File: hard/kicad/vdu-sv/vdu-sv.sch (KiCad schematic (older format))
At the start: 36 parts, among them J1 IOx, J2 (S)VGA, J3 IOx, U1 74HC138, U10 74HC245, U11 74HC245, U12 74HC245, U13 74HC574, U14 74HC157, U15 74HC86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

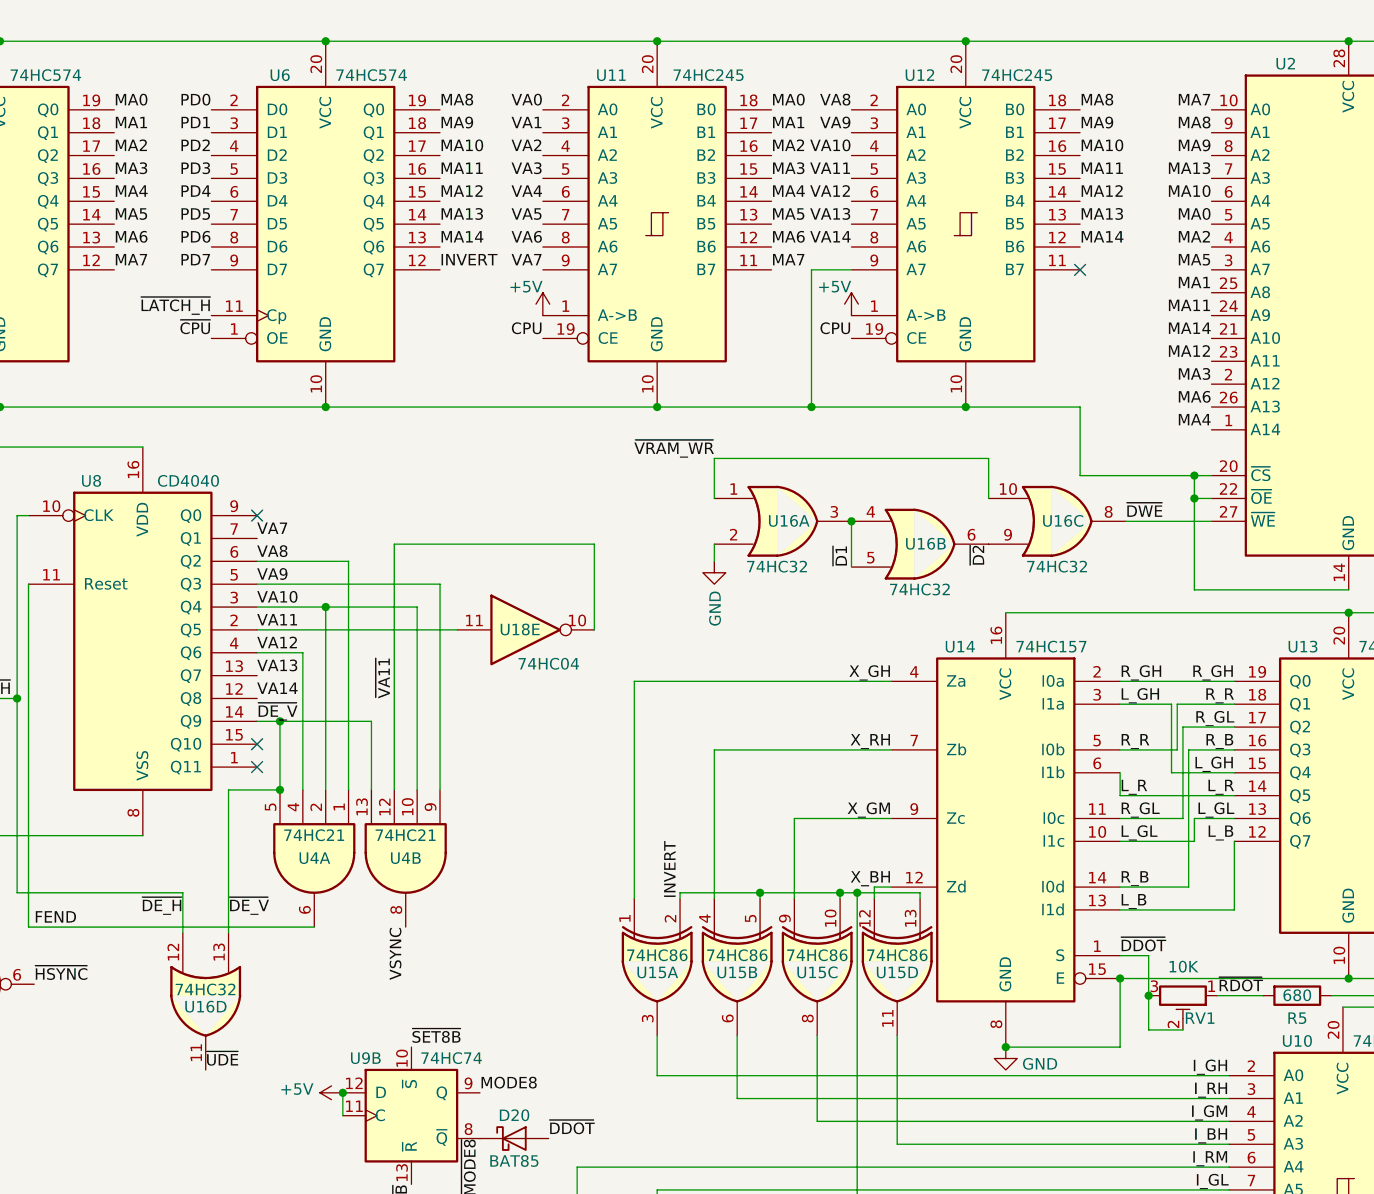
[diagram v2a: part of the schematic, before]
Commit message: upper nybble inverter shuffling
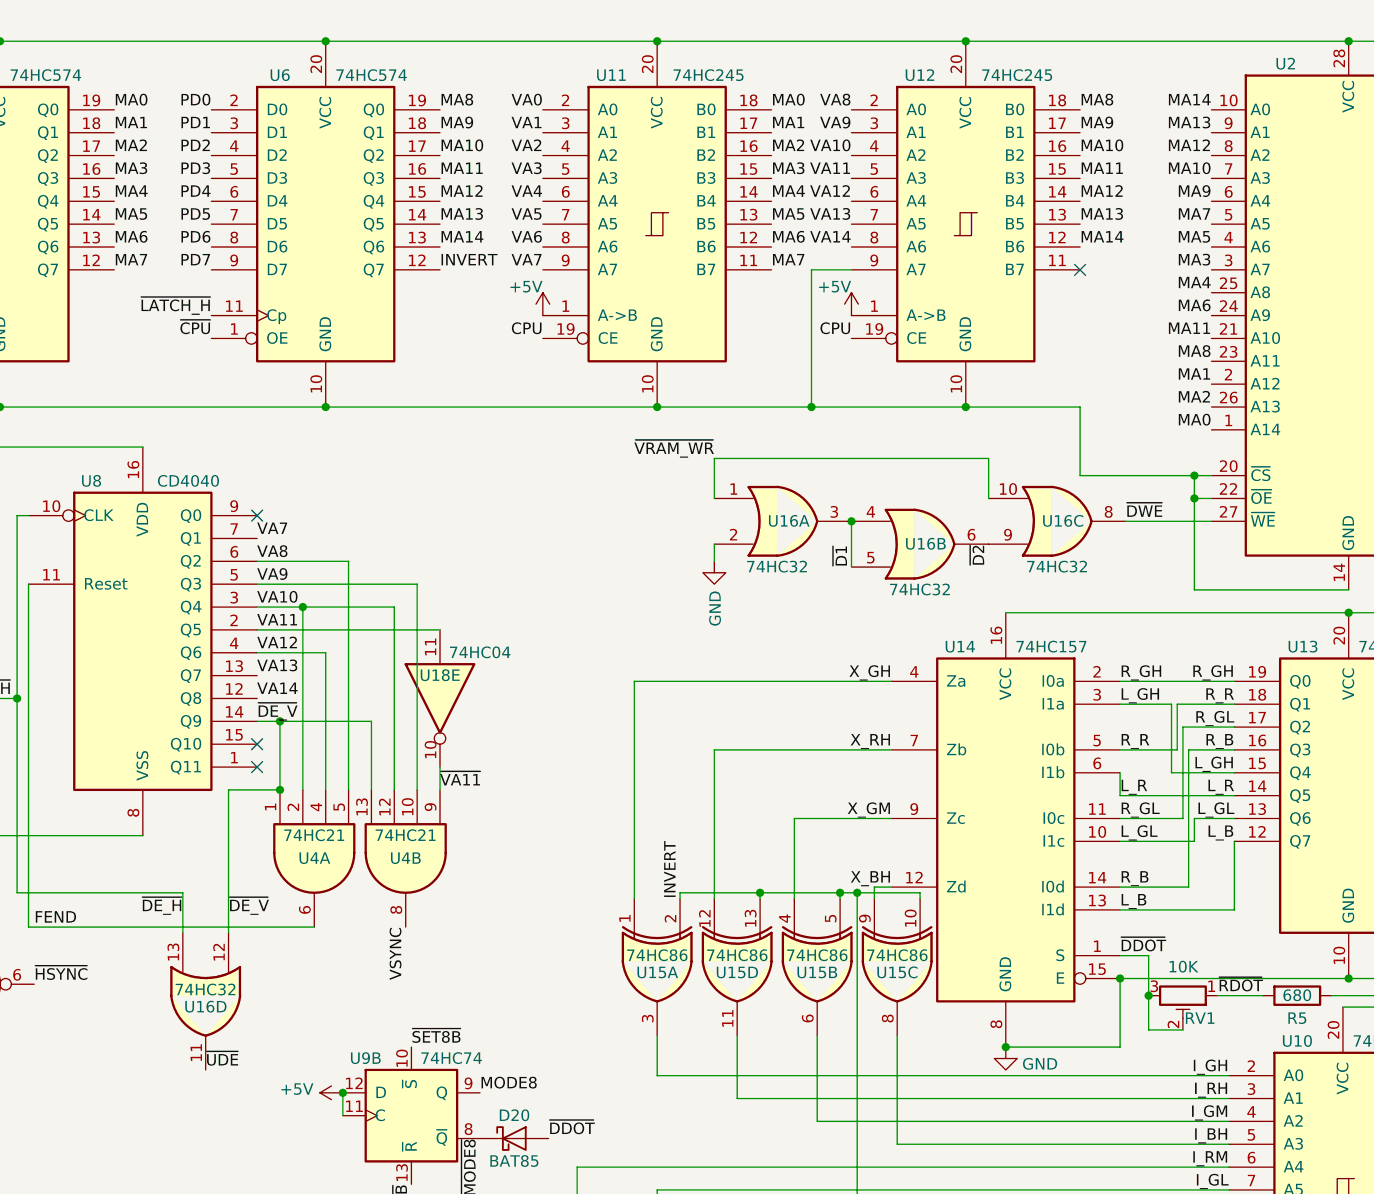
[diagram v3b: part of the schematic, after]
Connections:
- net I_BH: now also U15.8; no longer U15.11
- net I_GM: now also U15.6; no longer U15.8
- net I_RH: now also U15.11; no longer U15.6
- net MA0: now also U2.1 (A14); no longer U2.5 (A5)
- net MA1: now also U2.2 (A12); no longer U2.25 (A8)
- net MA10: now also U2.7 (A3); no longer U2.6 (A4)
- net MA11: now also U2.21 (A10); no longer U2.24 (A9)
- net MA12: now also U2.8 (A2); no longer U2.23 (A11)
- net MA13: now also U2.9 (A1); no longer U2.7 (A3)
- net MA14: now also U2.10 (A0); no longer U2.21 (A10)
- net MA2: now also U2.26 (A13); no longer U2.4 (A6)
- net MA3: now also U2.3 (A7); no longer U2.2 (A12)
- net MA4: now also U2.25 (A8); no longer U2.1 (A14)
- net MA5: now also U2.4 (A6); no longer U2.3 (A7)
- net MA6: now also U2.24 (A9); no longer U2.26 (A13)
- net MA7: now also U2.5 (A5); no longer U2.10 (A0)
- net MA8: now also U2.23 (A11); no longer U2.9 (A1)
- net MA9: now also U2.6 (A4); no longer U2.8 (A2)
- net VA10: now also U4.12; no longer U4.10
- net VA8: now also U4.5; no longer U4.1
- net VA9: now also U4.10; no longer U4.9
- net X_BH: now also U15.9; no longer U15.12
- net X_GM: now also U15.4; no longer U15.9
- net X_RH: now also U15.12; no longer U15.4
- net ~DE_H: now also U16.13; no longer U16.12
- net ~DE_V: now also U16.12, U4.1; no longer U16.13, U4.5
- net ~VA11: now also U4.9; no longer U4.12
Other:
- moved on the sheet: U15B, U15C, U15D, U18E

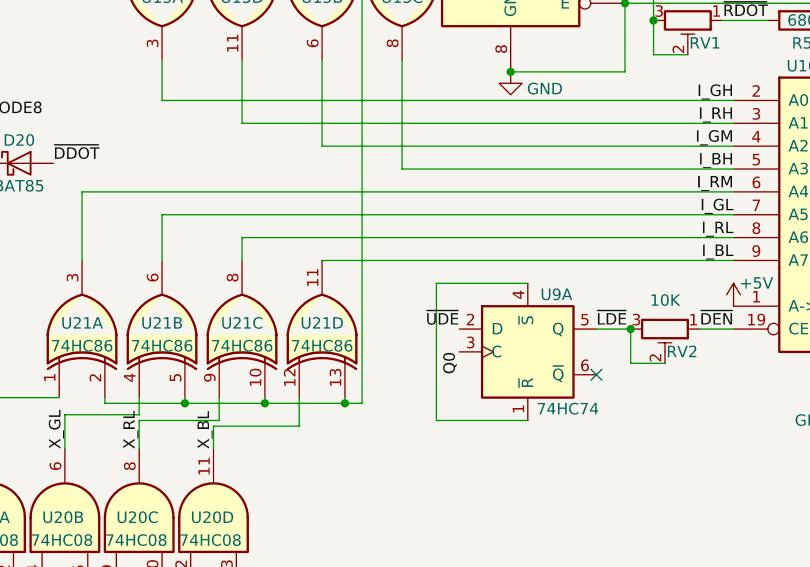
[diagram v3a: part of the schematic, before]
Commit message: somewhat more compact VDU-SV
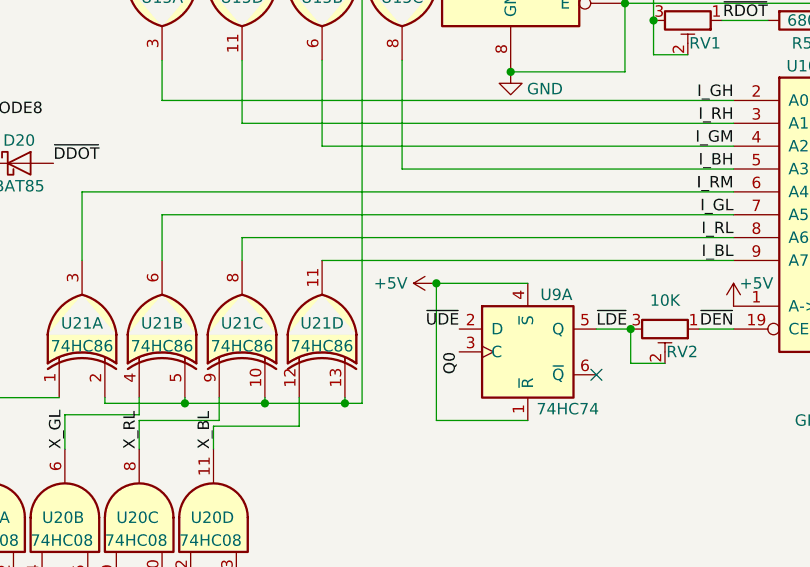
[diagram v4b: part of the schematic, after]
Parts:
- D20: footprint Diode_THT:D_DO-35_SOD27_P7.62mm_Horizontal -> Diode_THT:D_DO-35_SOD27_P2.54mm_Vertical_KathodeUp
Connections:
- net +5V: now also U9.1 (~R), U9.4 (~S)
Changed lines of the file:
@@
 F 0 "D20" H 5975 5475 50  0000 C CNN
 F 1 "BAT85" H 5975 5275 50  0000 C CNN
-F 2 "Diode_THT:D_DO-35_SOD27_P7.62mm_Horizontal" H 5975 5200 50  0001 C CNN
+F 2 "Diode_THT:D_DO-35_SOD27_P2.54mm_Vertical_KathodeUp" H 5975 5200 50  0001 C CNN
 F 3 "https://assets.nexperia.com/documents/data-sheet/BAT85.pdf" H 5975 5375 50  0001 C CNN
 	1    5975 5375
@@
 Text Label 9100 5100 2    50   ~ 0
 I_GH
+$Comp
+L power:+5V #PWR0115
+U 1 1 65A6B7BC
+P 7800 5900
+F 0 "#PWR0115" H 7800 5750 50  0001 C CNN
+F 1 "+5V" V 7800 6100 50  0000 C CNN
+F 2 "" H 7800 5900 50  0001 C CNN
+F 3 "" H 7800 5900 50  0001 C CNN
+	1    7800 5900
+	0    -1   -1   0
+$EndComp
+Connection ~ 7800 5900
 $EndSCHEMATC

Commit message: even more compact VDU-SV
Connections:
- net C320: now also U3.9; no longer U3.5
- net CPU: now also U3.11; no longer U3.3
- net DOT: now also U3.3; no longer U3.11
- net Q0: now also U3.1; no longer U3.13
- net VA5: now also U3.4; no longer U3.10
- net ~C320: now also U3.6; no longer U3.8
- net ~CPU: now also U3.2; no longer U3.12
- net ~DE_H: now also U3.5; no longer U3.9
- net ~HSYNC: now also U3.8; no longer U3.6
- net ~VA6: now also U3.10; no longer U3.4
- net ~VRAM_RD: now also U3.12; no longer U3.2
- net ~VRAM_WR: now also U3.13; no longer U3.1
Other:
- moved on the sheet: U3A, U3B, U3C, U3D
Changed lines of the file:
@@
 L 74xx:74LS00 U3
 U 1 1 65A53EB2
+P 1225 5250
+F 0 "U3" H 1200 5250 50  0000 C CNN
+F 1 "74HC00" H 1200 5050 50  0000 C CNN
+F 2 "Package_DIP:DIP-14_W7.62mm_Socket" H 1225 5250 50  0001 C CNN
+F 3 "http://www.ti.com/lit/gpn/sn74ls00" H 1225 5250 50  0001 C CNN
+	1    1225 5250
+	1    0    0    -1
+$EndComp
+$Comp
+L 74xx:74LS00 U3
+U 2 1 65A55B68
+P 2675 4500
+F 0 "U3" H 2650 4500 50  0000 C CNN
+F 1 "74HC00" H 2675 4300 50  0000 C CNN
+F 2 "Package_DIP:DIP-14_W7.62mm_Socket" H 2675 4500 50  0001 C CNN
+F 3 "http://www.ti.com/lit/gpn/sn74ls00" H 2675 4500 50  0001 C CNN
+	2    2675 4500
+	0    1    1    0
+$EndComp
+$Comp
+L 74xx:74LS00 U3
+U 4 1 65A58ED5
 P 1225 5875
 F 0 "U3" H 1200 5875 50  0000 C CNN
-F 1 "74HC00" H 1200 5675 50  0000 C CNN
+F 1 "74HC00" H 1225 6075 50  0000 C CNN
 F 2 "Package_DIP:DIP-14_W7.62mm_Socket" H 1225 5875 50  0001 C CNN
 F 3 "http://www.ti.com/lit/gpn/sn74ls00" H 1225 5875 50  0001 C CNN
-	1    1225 5875
-	1    0    0    -1
-$EndComp
-$Comp
-L 74xx:74LS00 U3
-U 2 1 65A55B68
-P 3575 4700
-F 0 "U3" H 3550 4700 50  0000 C CNN
-F 1 "74HC00" H 3575 4500 50  0000 C CNN
-F 2 "Package_DIP:DIP-14_W7.62mm_Socket" H 3575 4700 50  0001 C CNN
-F 3 "http://www.ti.com/lit/gpn/sn74ls00" H 3575 4700 50  0001 C CNN
-	2    3575 4700
-	1    0    0    -1
-$EndComp
-$Comp
-L 74xx:74LS00 U3
-U 3 1 65A56322
-P 2675 4500
-F 0 "U3" V 2650 4500 50  0000 C CNN
-F 1 "74HC00" V 2575 4500 50  0000 C CNN
-F 2 "Package_DIP:DIP-14_W7.62mm_Socket" H 2675 4500 50  0001 C CNN
-F 3 "http://www.ti.com/lit/gpn/sn74ls00" H 2675 4500 50  0001 C CNN
-	3    2675 4500
-	0    -1   1    0
-$EndComp
-$Comp
-L 74xx:74LS00 U3
-U 4 1 65A58ED5
-P 1225 5250
-F 0 "U3" H 1200 5250 50  0000 C CNN
-F 1 "74HC00" H 1225 5450 50  0000 C CNN
-F 2 "Package_DIP:DIP-14_W7.62mm_Socket" H 1225 5250 50  0001 C CNN
-F 3 "http://www.ti.com/lit/gpn/sn74ls00" H 1225 5250 50  0001 C CNN
-	4    1225 5250
+	4    1225 5875
 	1    0    0    1
 $EndComp
@@
 $EndComp
 Connection ~ 7800 5900
+$Comp
+L 74xx:74LS00 U3
+U 3 1 65A56322
+P 3575 4700
+F 0 "U3" V 3550 4700 50  0000 C CNN
+F 1 "74HC00" V 3475 4700 50  0000 C CNN
+F 2 "Package_DIP:DIP-14_W7.62mm_Socket" H 3575 4700 50  0001 C CNN
+F 3 "http://www.ti.com/lit/gpn/sn74ls00" H 3575 4700 50  0001 C CNN
+	3    3575 4700
+	1    0    0    1
+$EndComp
 $EndSCHEMATC

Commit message: some reposition
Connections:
- net BA2: now also U18.9; no longer U18.13
- net C320: now also U18.6; no longer U18.8
- net DOT: now also U18.11; no longer U18.5
- net VA11: now also U18.13; no longer U18.11
- net ~BA2: now also U18.8; no longer U18.12
- net ~C320: now also U18.5; no longer U18.9
- net ~DOT: now also R5.2, U18.10; no longer R5.1, U18.6
- net ~RDOT: now also R5.1; no longer R5.2
- net ~VA11: now also U18.12; no longer U18.10
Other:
- moved on the sheet: U18C, U18D, U18E, U18F
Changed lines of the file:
@@
 L 74xx:74HC04 U18
 U 3 1 65AEE968
+P 2975 4800
+F 0 "U18" H 2850 4800 50  0000 L CNN
+F 1 "74HC04" H 2850 4625 50  0000 L CNN
+F 2 "Package_DIP:DIP-14_W7.62mm_Socket" H 2975 4800 50  0001 C CNN
+F 3 "https://assets.nexperia.com/documents/data-sheet/74HC_HCT04.pdf" H 2975 4800 50  0001 C CNN
+	3    2975 4800
+	1    0    0    -1
+$EndComp
+$Comp
+L 74xx:74HC04 U18
+U 4 1 65AEFD06
+P 1825 4625
+F 0 "U18" H 1800 4625 50  0000 C CNN
+F 1 "74HC04" H 1850 4450 50  0000 C CNN
+F 2 "Package_DIP:DIP-14_W7.62mm_Socket" H 1825 4625 50  0001 C CNN
+F 3 "https://assets.nexperia.com/documents/data-sheet/74HC_HCT04.pdf" H 1825 4625 50  0001 C CNN
+	4    1825 4625
+	1    0    0    -1
+$EndComp
+$Comp
+L 74xx:74HC04 U18
+U 5 1 65AF115C
 P 1825 5250
-F 0 "U18" H 1700 5250 50  0000 L CNN
-F 1 "74HC04" H 1700 5075 50  0000 L CNN
+F 0 "U18" H 1800 5250 50  0000 C CNN
+F 1 "74HC04" H 1875 5425 50  0000 C CNN
 F 2 "Package_DIP:DIP-14_W7.62mm_Socket" H 1825 5250 50  0001 C CNN
 F 3 "https://assets.nexperia.com/documents/data-sheet/74HC_HCT04.pdf" H 1825 5250 50  0001 C CNN
-	3    1825 5250
-	1    0    0    -1
-$EndComp
-$Comp
-L 74xx:74HC04 U18
-U 4 1 65AEFD06
-P 2975 4800
-F 0 "U18" H 2950 4800 50  0000 C CNN
-F 1 "74HC04" H 3000 4625 50  0000 C CNN
-F 2 "Package_DIP:DIP-14_W7.62mm_Socket" H 2975 4800 50  0001 C CNN
-F 3 "https://assets.nexperia.com/documents/data-sheet/74HC_HCT04.pdf" H 2975 4800 50  0001 C CNN
-	4    2975 4800
-	1    0    0    -1
-$EndComp
-$Comp
-L 74xx:74HC04 U18
-U 5 1 65AF115C
+	5    1825 5250
+	1    0    0    1
+$EndComp
+$Comp
+L 74xx:74HC04 U18
+U 6 1 65AF2AF3
 P 5650 3450
 F 0 "U18" V 5550 3450 50  0000 C CNN
-F 1 "74HC04" V 5450 3275 50  0000 C CNN
+F 1 "74HC04" V 5450 3625 50  0000 C CNN
 F 2 "Package_DIP:DIP-14_W7.62mm_Socket" H 5650 3450 50  0001 C CNN
 F 3 "https://assets.nexperia.com/documents/data-sheet/74HC_HCT04.pdf" H 5650 3450 50  0001 C CNN
-	5    5650 3450
-	0    -1   1    0
-$EndComp
-$Comp
-L 74xx:74HC04 U18
-U 6 1 65AF2AF3
-P 1825 4625
-F 0 "U18" H 1800 4625 50  0000 C CNN
-F 1 "74HC04" H 1825 4851 50  0000 C CNN
-F 2 "Package_DIP:DIP-14_W7.62mm_Socket" H 1825 4625 50  0001 C CNN
-F 3 "https://assets.nexperia.com/documents/data-sheet/74HC_HCT04.pdf" H 1825 4625 50  0001 C CNN
-	6    1825 4625
-	1    0    0    -1
+	6    5650 3450
+	0    1    1    0
 $EndComp
 $Comp
@@
 U 1 1 65A6028D
 P 9400 4750
-F 0 "R5" V 9500 4750 50  0000 C CNN
+F 0 "R5" V 9300 4750 50  0000 C CNN
 F 1 "680" V 9400 4750 50  0000 C CNN
 F 2 "Resistor_THT:R_Axial_DIN0207_L6.3mm_D2.5mm_P2.54mm_Vertical" V 9330 4750 50  0001 C CNN
 F 3 "~" H 9400 4750 50  0001 C CNN
 	1    9400 4750
-	0    1    1    0
+	0    -1   -1   0
 $EndComp
 Text Label 6125 5375 0    50   ~ 0
